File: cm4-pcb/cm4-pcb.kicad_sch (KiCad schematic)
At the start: 37 parts, among them J1 Conn_01x02_Pin, J2 Conn_01x02_Pin, J3 USB1125-GF-B, J4 Conn_02x03_Odd_Even, J5 Conn_01x04, J6 J0011D21NL, J7 Conn_01x02, J8 Conn_01x02, J9 Conn_01x02_Pin, U1 Pfostenstecker_6_2x3, U2 Pfostenstecker_6_2x3, U5 SMD-PUSH-BTN

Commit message: JLCPCB Assemly
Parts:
- removed D1, D2, D3, D4: ESD122DMYR, ESD122DMYR, symbol ESD122DMYR:ESD122DMYR
- added U3, U4, U6, U7: ESD122DMYR, BohleBots:X2SON-3_L1.3-W0.6-L, symbol bohlebots.lib:ESD122DMYR
- Module1: LCSC (none) -> C424649
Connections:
- net GND: now also U3.1 (GND), U4.1 (GND), U6.1 (GND), U7.1 (GND)
- net SCL: now also U7.3 (IO2)
- net SDA: now also U7.2 (IO1)
- net TRD0_N: now also U3.2 (IO1)
- net TRD0_P: now also U3.3 (IO2)
- net TRD1_N: now also U4.2 (IO1)
- net TRD1_P: now also U4.3 (IO2)
- net USB_D+: now also U6.3 (IO2)
- net USB_D-: now also U6.2 (IO1)

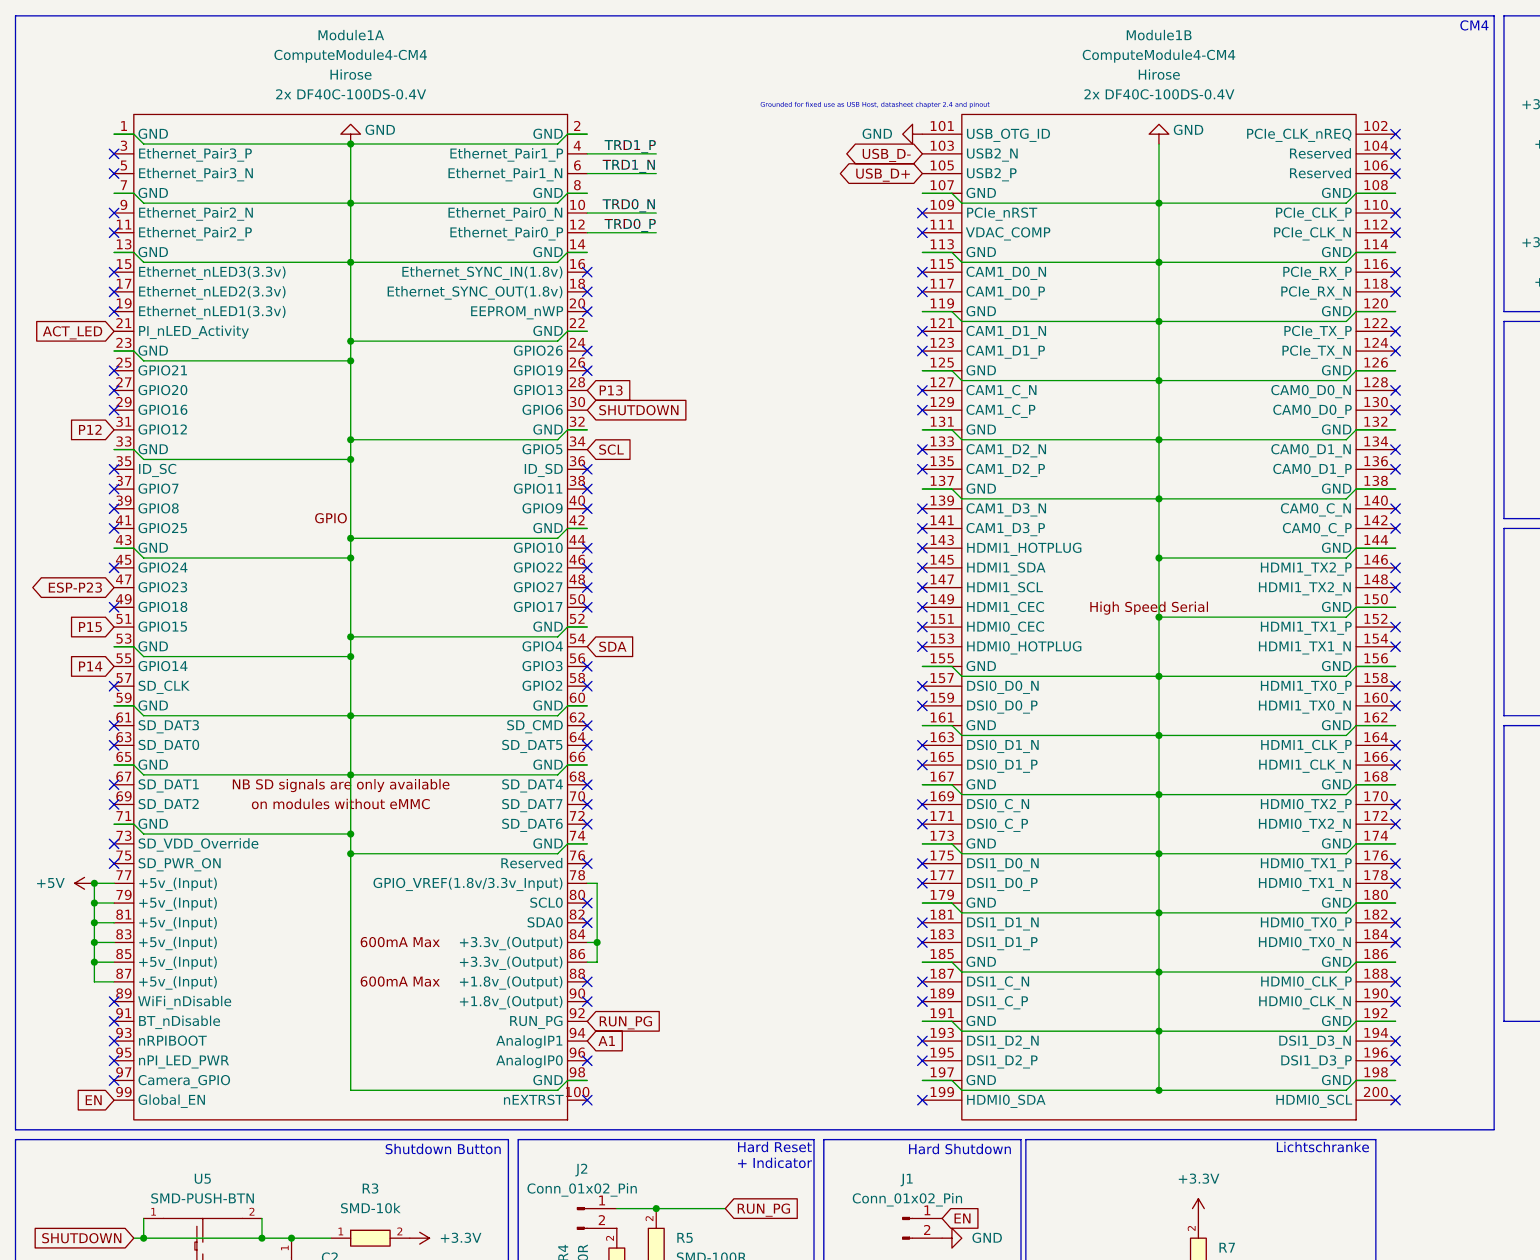
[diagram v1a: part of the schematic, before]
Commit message: Fixed connections for cm4 connectors
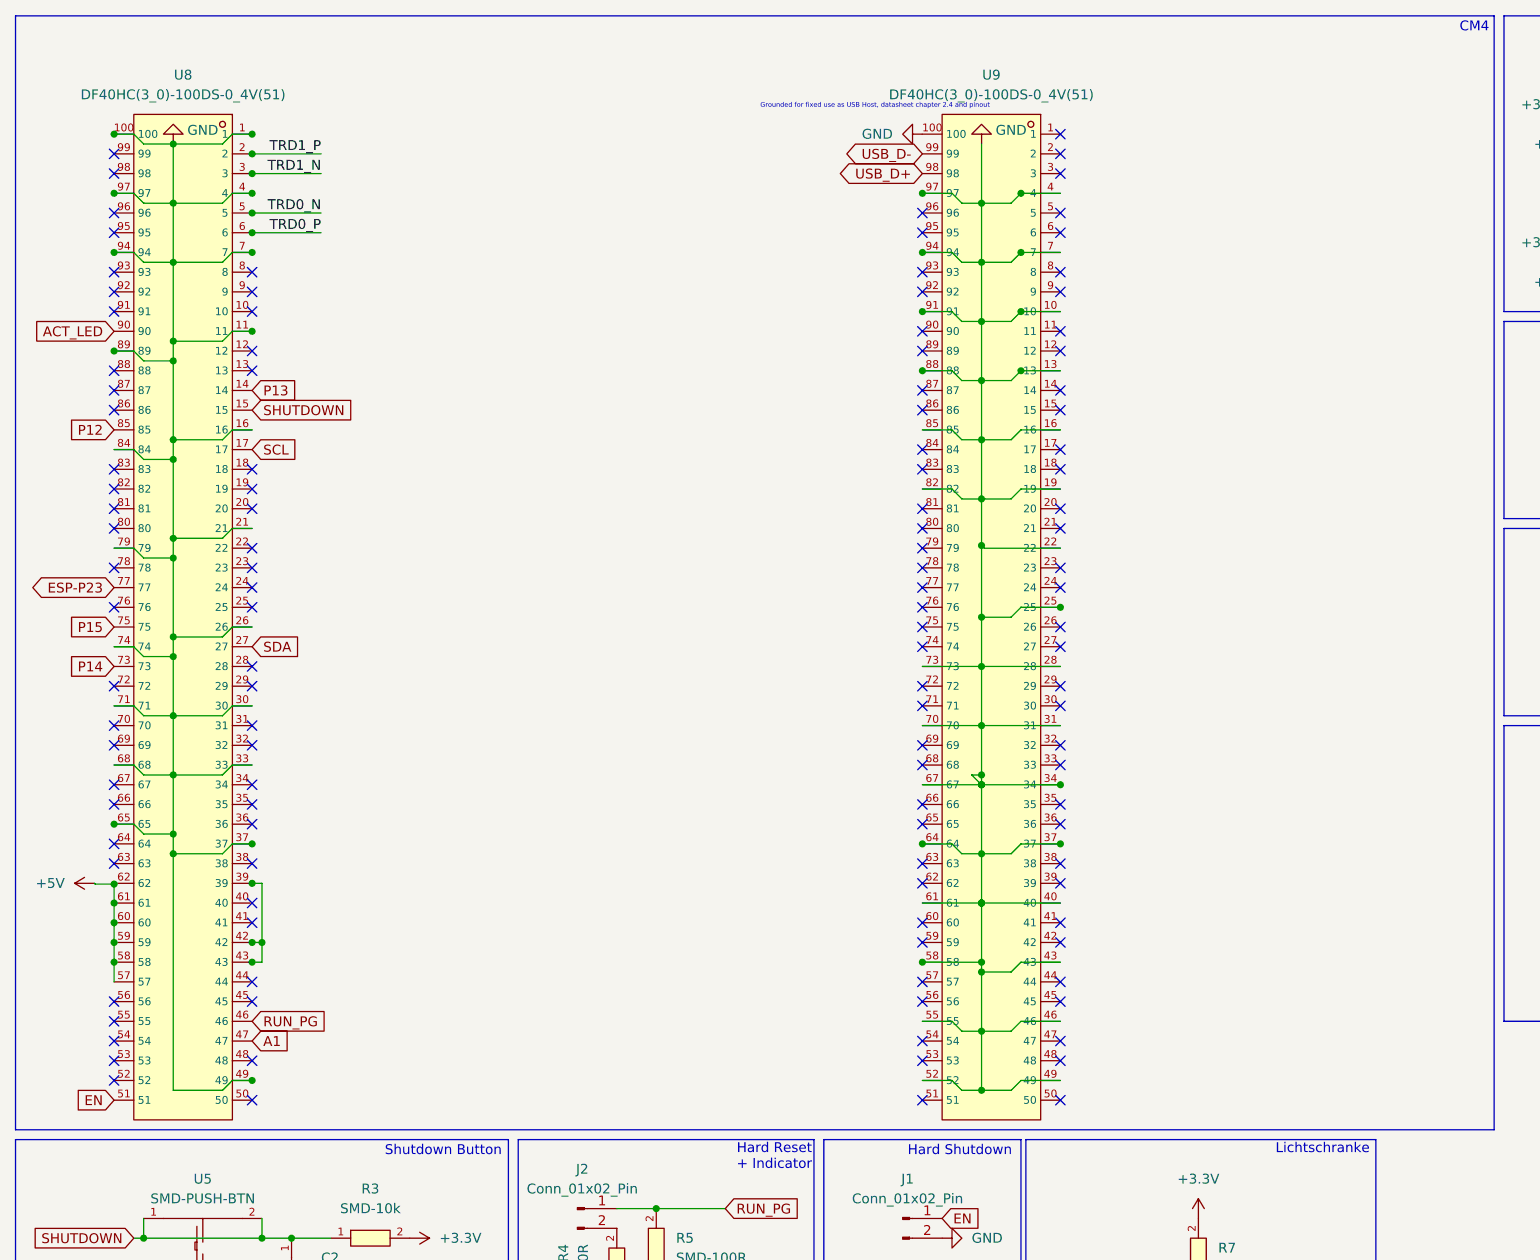
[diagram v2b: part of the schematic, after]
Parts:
- removed Module1: ComputeModule4-CM4, CM4IO:Raspberry-Pi-4-Compute-Module, symbol CM4IO:ComputeModule4-CM4
- added U8, U9: DF40HC(3_0)-100DS-0_4V(51), BohleBots:CONN-SMD_DF40HC-3.0-100DS-0.4V-51, symbol bohlebots.lib:DF40HC(3_0)-100DS-0_4V(51)
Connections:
- net +5V: now also U8.57, U8.58, U8.59, U8.60, U8.61, U8.62
- net A1: now also U8.47
- net ACT_LED: now also U8.90
- net EN: now also U8.51
- net ESP-P23: now also U8.77
- net GND: now also U8.1, U8.100, U8.11, U8.16, U8.21, U8.26, U8.30, U8.33, U8.37, U8.4, U8.49, U8.68, U8.7, U8.71, U8.74, U8.79, U8.84, U8.89, U8.94, U9.10, U9.100, U9.13, U9.16, U9.19, U9.22, U9.25, U9.28, U9.31, U9.34, U9.37, U9.4, U9.40, U9.43, U9.46, U9.49, U9.52, U9.55, U9.58, U9.61, U9.67, U9.7, U9.70, U9.73, U9.82, U9.85, U9.88, U9.91, U9.94, U9.97
- net P12: now also U8.85
- net P13: now also U8.14
- net P14: now also U8.73
- net P15: now also U8.75
- net RUN_PG: now also U8.46
- net SCL: now also U8.17
- net SDA: now also U8.27
- net SHUTDOWN: now also U8.15
- net TRD0_N: now also U8.5
- net TRD0_P: now also U8.6
- net TRD1_N: now also U8.3
- net TRD1_P: now also U8.2
- net USB_D+: now also U9.98
- net USB_D-: now also U9.99
- new net: U8.39, U8.42, U8.43

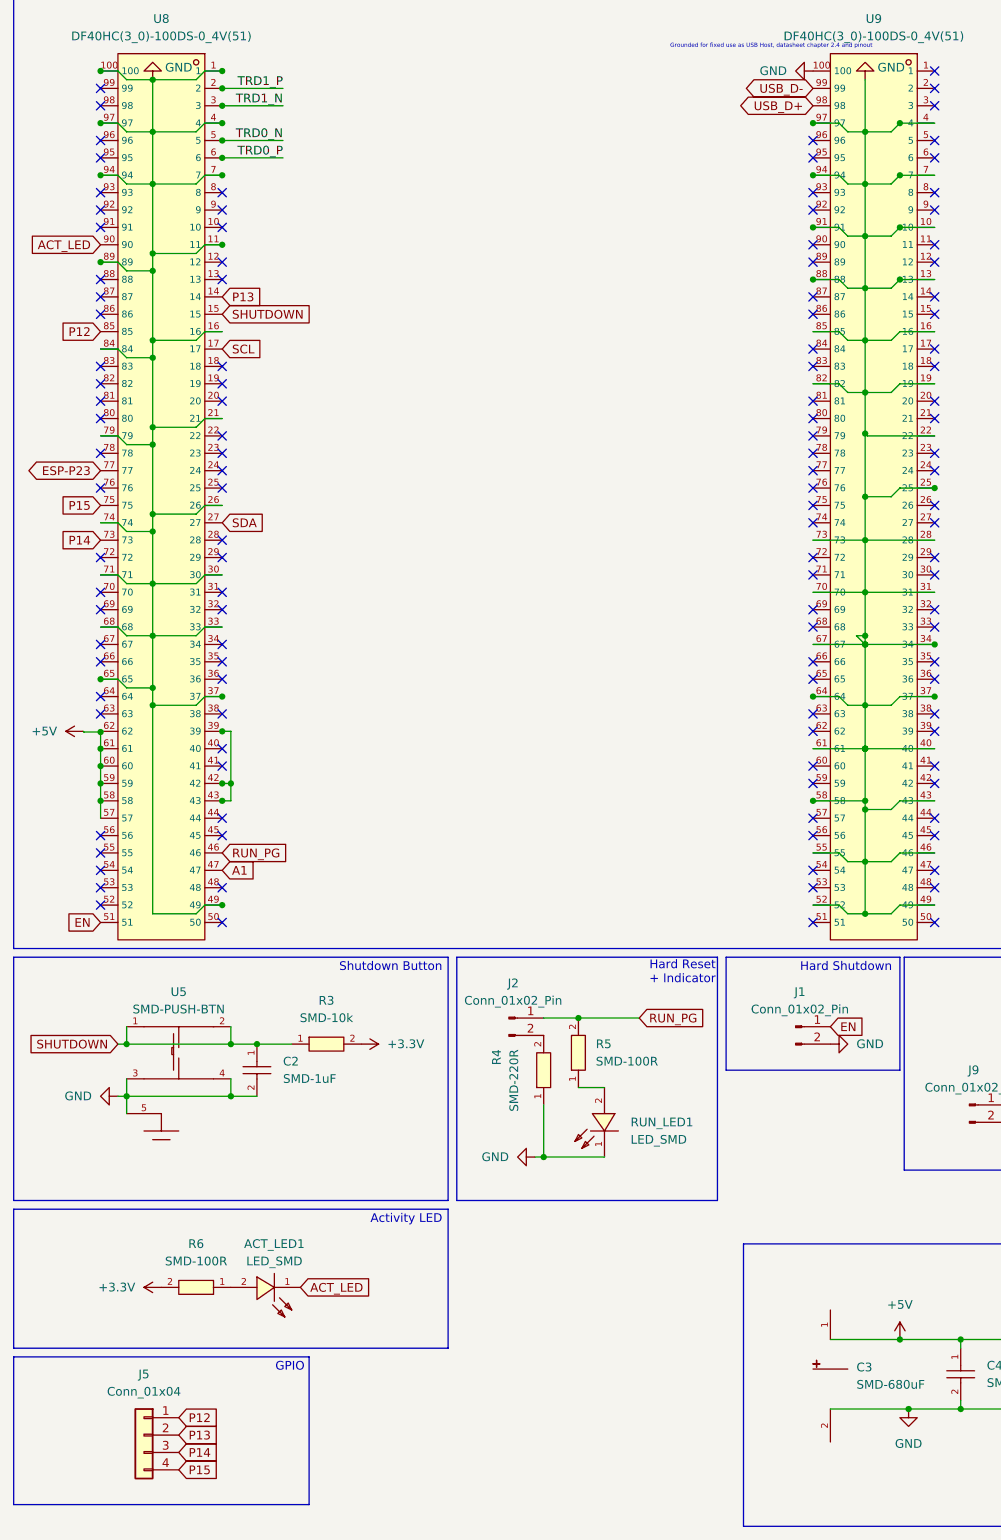
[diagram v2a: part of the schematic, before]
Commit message: Changed cm4 connectors + some solder pads
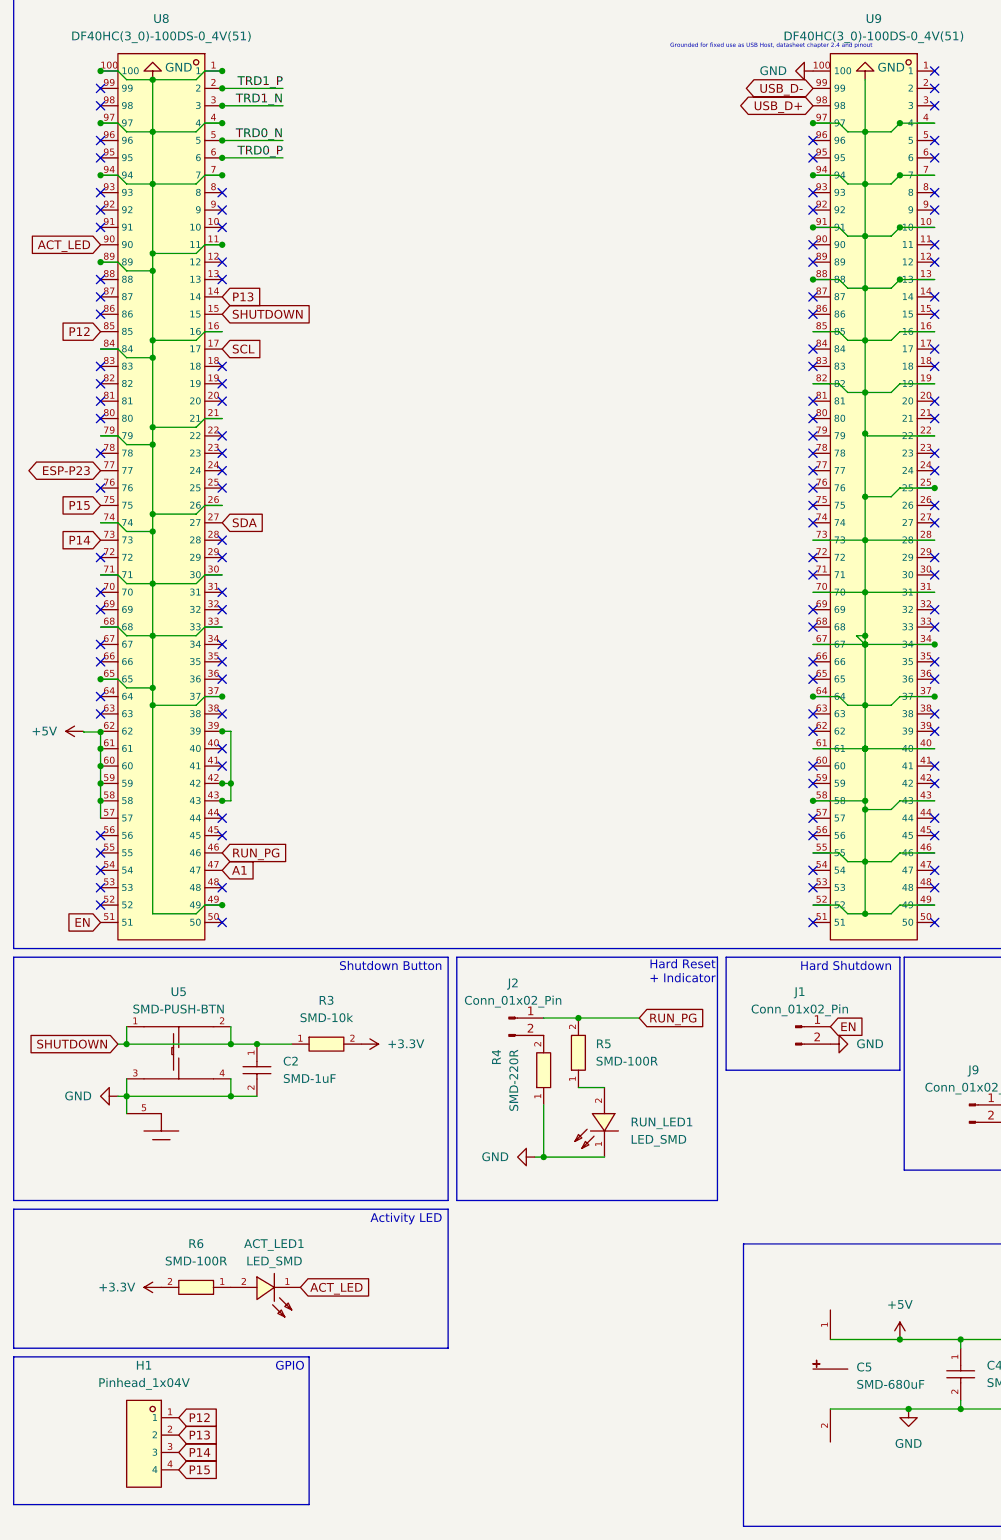
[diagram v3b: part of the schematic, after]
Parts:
- removed C3: SMD-680uF, BohleBots:CAP-SMD_BD10.0-L10.3-W10.3-LS11.3-FD, symbol bohlebots.lib:SMD-680uF
- removed J5: Conn_01x04, Connector_PinSocket_2.54mm:PinSocket_1x04_P2.54mm_Vertical, symbol Connector_Generic:Conn_01x04
- added C5: SMD-680uF, BohleBots:CAP-SMD_BD10.0-L10.3-W10.3-LS11.3-FD, symbol bohlebots.lib:SMD-680uF
- added H1: Pinhead_1x04V, BohleBots:HDR-TH_4P-P2.54-V-M-1, symbol bohlebots.lib:Pinhead_1x04V
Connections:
- net +5V: now also C5.1
- net GND: now also U8.65, U8.97, U9.64, C5.2
- net P12: now also H1.1
- net P13: now also H1.2
- net P14: now also H1.3
- net P15: now also H1.4
